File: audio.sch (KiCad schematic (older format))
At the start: 4 parts

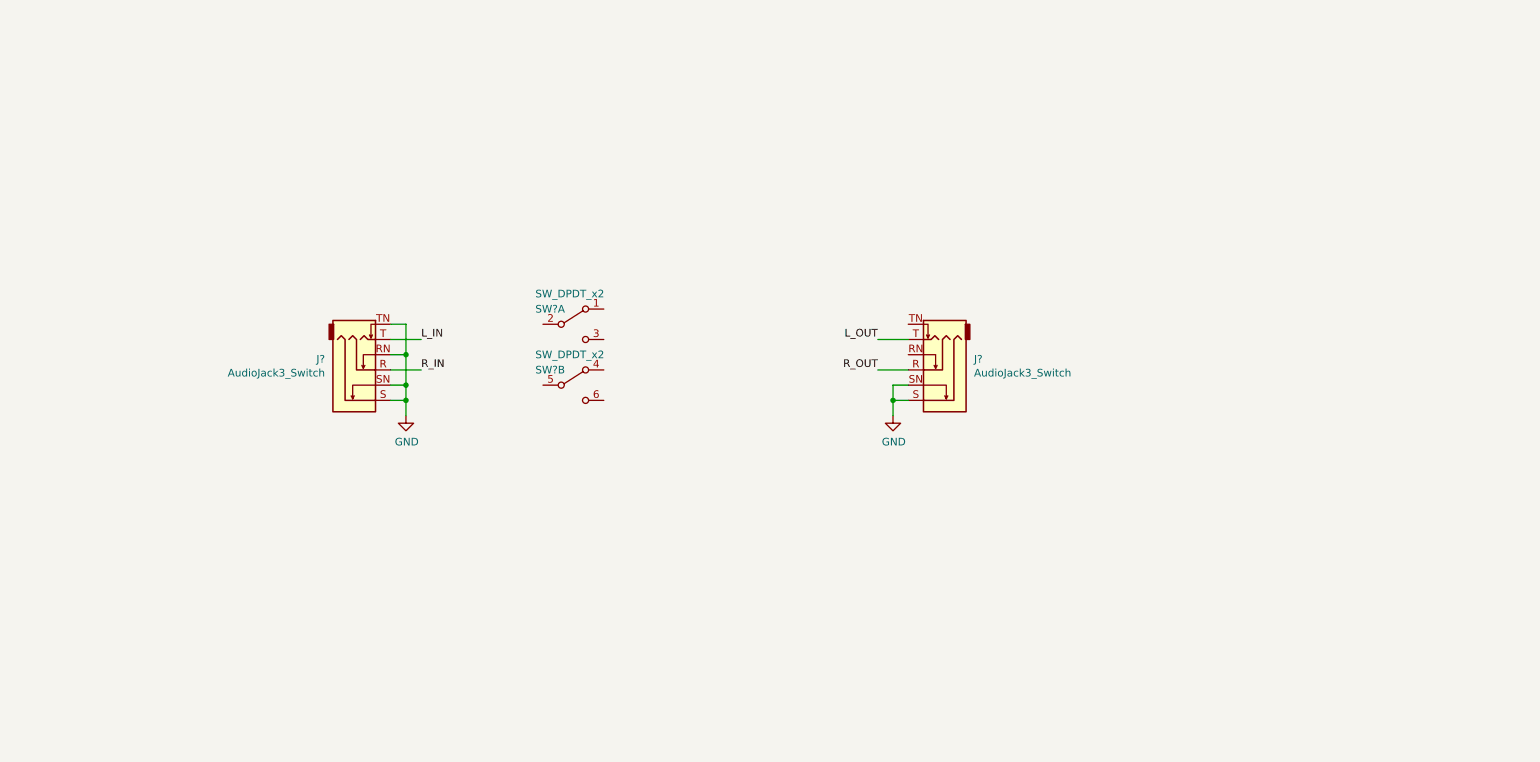
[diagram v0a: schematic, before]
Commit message: flesh out audio amp sheet, without R/C values
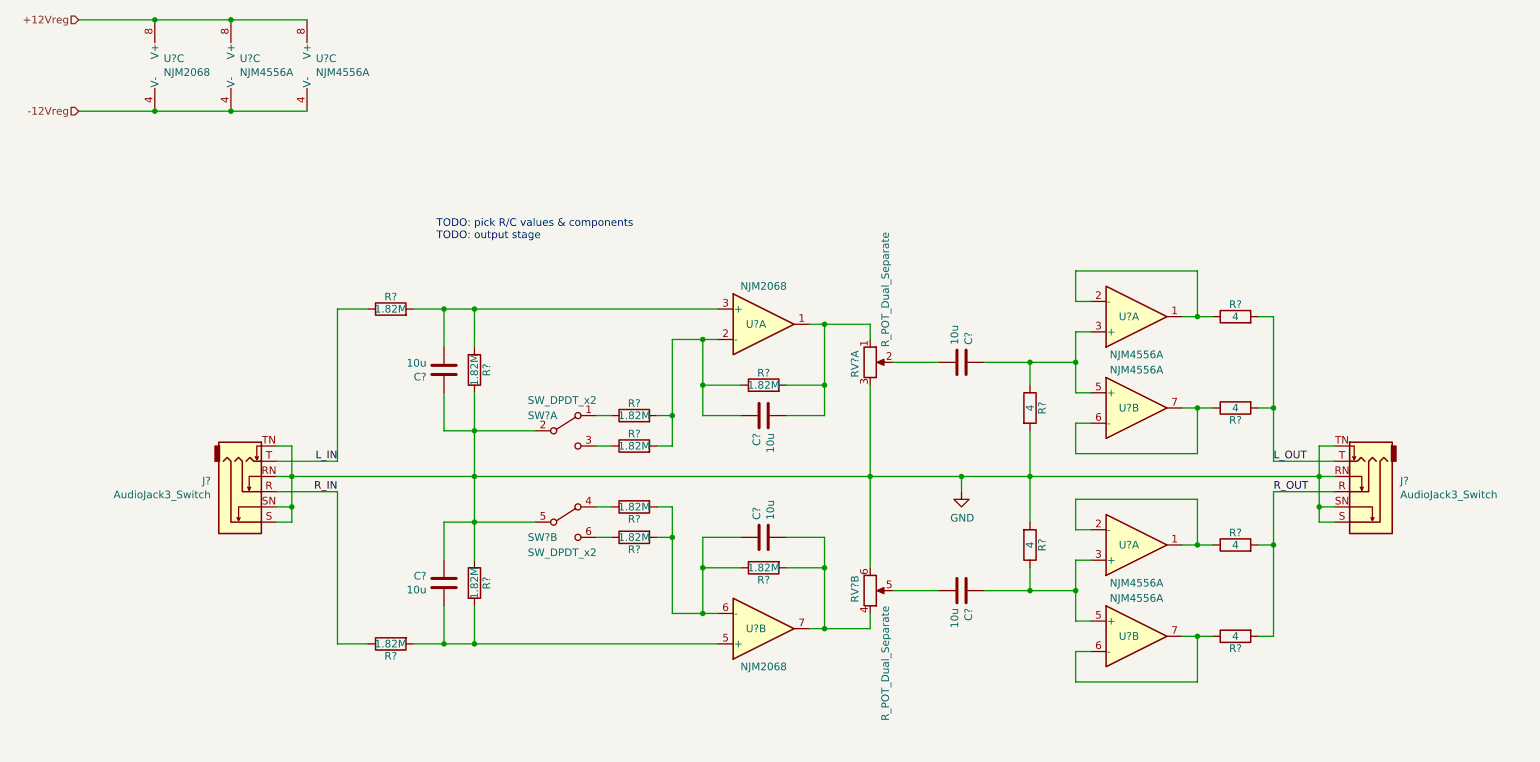
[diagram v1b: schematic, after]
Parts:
- added C? (x6): 10u, symbol Device:C
- added R? (x10): 1.82M, Resistor_SMD:R_0805_2012Metric_Pad1.15x1.40mm_HandSolder, symbol Device:R
- added R? (x6): 4, Resistor_SMD:R_0805_2012Metric_Pad1.15x1.40mm_HandSolder, symbol Device:R
- added RV? (x2): R_POT_Dual_Separate, symbol Device:R_POT_Dual_Separate
- added U? (x6): NJM4556A, symbol Amplifier_Operational:NJM4556A
- added U? (x3): NJM2068, symbol njr:NJM2068
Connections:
- net GND: now also J?.RN, J?.TN, SW?.2 (B), SW?.5 (B), C?.2, C?.2, R?.1, R?.1, R?.2, R?.2, RV?.3, RV?.6
- net L_IN: now also R?.1
- net L_OUT: now also R?.2, R?.2
- net R_IN: now also R?.1
- net R_OUT: now also R?.2, R?.2
- net at SW?.1 (A): now also R?.1
- net at SW?.3 (C): now also R?.1
- net at SW?.4 (A): now also R?.1
- net at SW?.6 (C): now also R?.1
- new net: R?.1, U?.1, U?.2 (-) (x2)
- new net: C?.2, R?.1, U?.3 (+), U?.5 (+) (x2)
- new net: R?.1, U?.6 (-), U?.7 (x2)
- new net: C?.1, R?.2, RV?.1, U?.1
- new net: C?.2, R?.1, R?.2, R?.2, U?.2 (-)
- new net: C?.1, R?.2, R?.2, U?.3 (+)
- new net: C?.1, R?.2, R?.2, U?.5 (+)
- new net: C?.2, R?.1, R?.2, R?.2, U?.6 (-)
- new net: C?.1, R?.2, RV?.4, U?.7
- new net: C?.1, RV?.2
- new net: C?.1, RV?.5
- new net +12Vreg: U?.8 (V+), U?.8 (V+), U?.8 (V+)
- new net -12Vreg: U?.4 (V-), U?.4 (V-), U?.4 (V-)
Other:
- note added: "TODO: pick R/C values & components\nTODO: output stage"
- moved on the sheet: J?, SW?A, SW?B

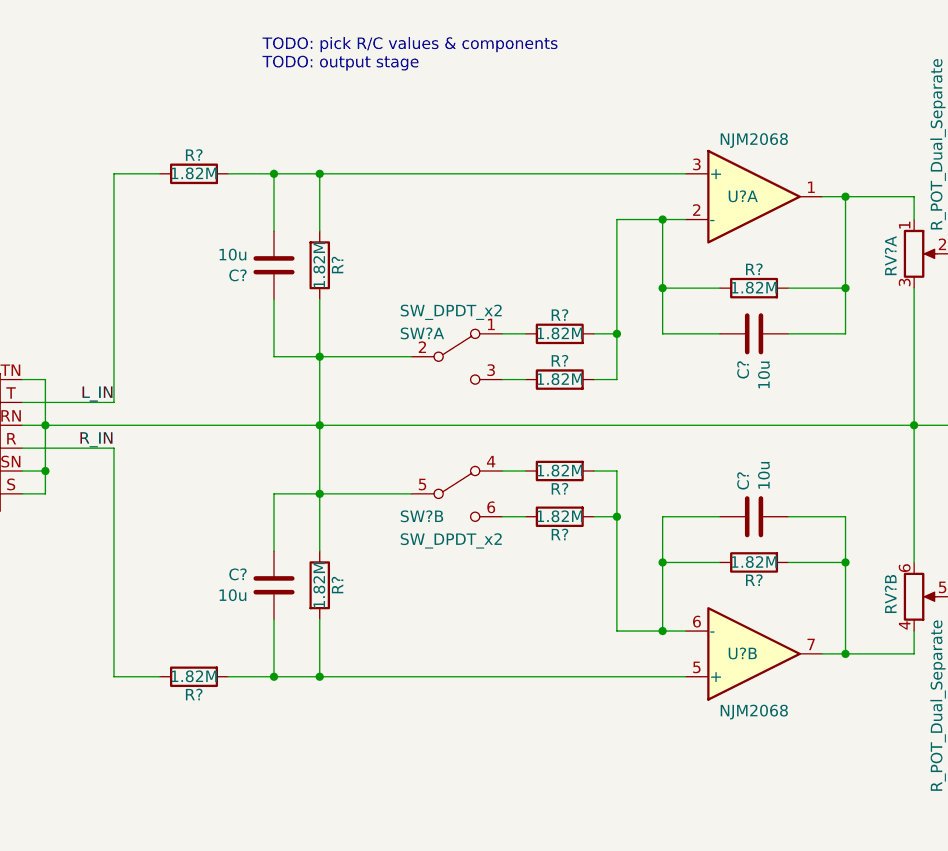
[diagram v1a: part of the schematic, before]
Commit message: add audio amp gain stage values
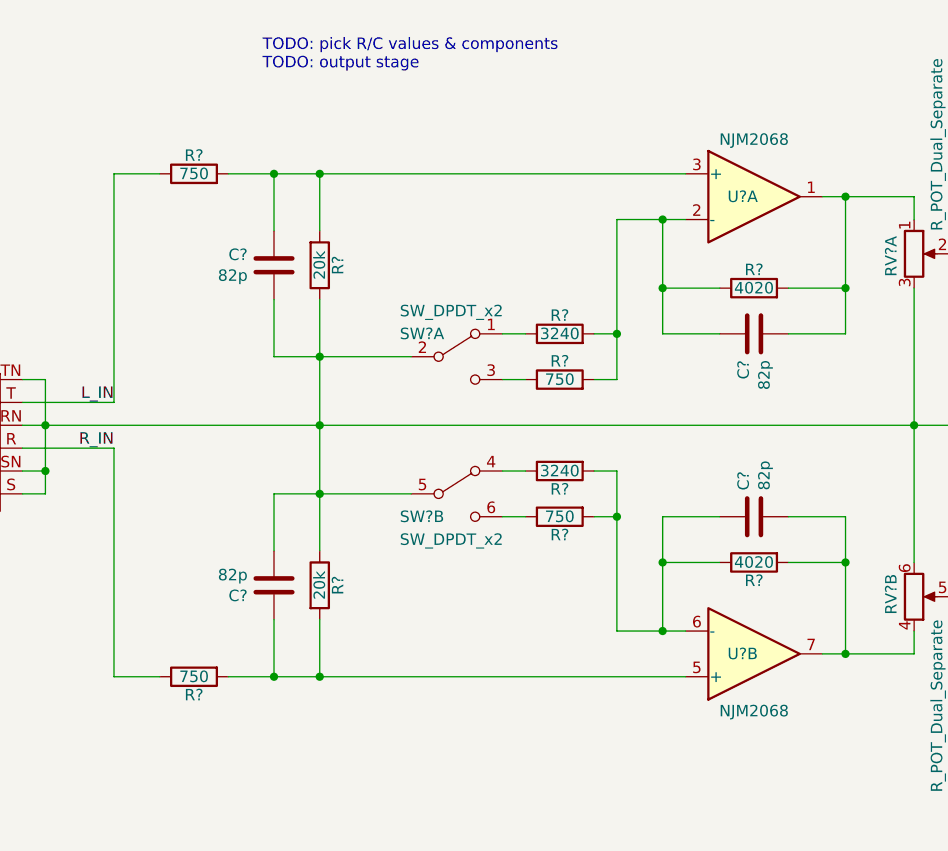
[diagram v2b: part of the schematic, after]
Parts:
- C? (x4): value 10u -> 82p
- R? (x2): value 1.82M -> 3240
- R? (x4): value 1.82M -> 750
- R? (x2): value 1.82M -> 4020
- R? (x2): value 1.82M -> 20k
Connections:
- net GND: now also C?.1, C?.1; no longer C?.2, C?.2
- net at R?.2, R?.2, U?.3 (+): now also C?.2; no longer C?.1
- net at R?.2, R?.2, U?.5 (+): now also C?.2; no longer C?.1
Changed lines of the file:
@@
 AR Path="/5CB56C16/5CE74784" Ref="R?"  Part="1"
 F 0 "R?" V 4830 3600 50  0000 C CNN
-F 1 "1.82M" V 4750 3600 50  0000 C CNN
+F 1 "3240" V 4750 3600 50  0000 C CNN
 F 2 "Resistor_SMD:R_0805_2012Metric_Pad1.15x1.40mm_HandSolder" V 4680 3600 50  0001 C CNN
 F 3 "https://industrial.panasonic.com/cdbs/www-data/pdf/RDA0000/AOA0000C304.pdf" H 4750 3600 50  0001 C CNN
@@
 AR Path="/5CB56C16/5CE74B22" Ref="R?"  Part="1"
 F 0 "R?" V 4830 3800 50  0000 C CNN
-F 1 "1.82M" V 4750 3800 50  0000 C CNN
+F 1 "750" V 4750 3800 50  0000 C CNN
 F 2 "Resistor_SMD:R_0805_2012Metric_Pad1.15x1.40mm_HandSolder" V 4680 3800 50  0001 C CNN
 F 3 "https://industrial.panasonic.com/cdbs/www-data/pdf/RDA0000/AOA0000C304.pdf" H 4750 3800 50  0001 C CNN
@@
 AR Path="/5CB56C16/5CE74BEC" Ref="R?"  Part="1"
 F 0 "R?" V 4830 4200 50  0000 C CNN
-F 1 "1.82M" V 4750 4200 50  0000 C CNN
+F 1 "3240" V 4750 4200 50  0000 C CNN
 F 2 "Resistor_SMD:R_0805_2012Metric_Pad1.15x1.40mm_HandSolder" V 4680 4200 50  0001 C CNN
 F 3 "https://industrial.panasonic.com/cdbs/www-data/pdf/RDA0000/AOA0000C304.pdf" H 4750 4200 50  0001 C CNN
@@
 AR Path="/5CB56C16/5CE74C54" Ref="R?"  Part="1"
 F 0 "R?" V 4830 4400 50  0000 C CNN
-F 1 "1.82M" V 4750 4400 50  0000 C CNN
+F 1 "750" V 4750 4400 50  0000 C CNN
 F 2 "Resistor_SMD:R_0805_2012Metric_Pad1.15x1.40mm_HandSolder" V 4680 4400 50  0001 C CNN
 F 3 "https://industrial.panasonic.com/cdbs/www-data/pdf/RDA0000/AOA0000C304.pdf" H 4750 4400 50  0001 C CNN
@@
 AR Path="/5CB56C16/5CE7733B" Ref="C?"  Part="1"
 F 0 "C?" H 5485 3554 50  0000 R CNN
-F 1 "10u" H 5485 3645 50  0000 R CNN
+F 1 "82p" H 5485 3645 50  0000 R CNN
 F 2 "" H 5638 3450 50  0001 C CNN
 F 3 "" H 5600 3600 50  0001 C CNN
@@
 AR Path="/5CB56C16/5CE77AE6" Ref="R?"  Part="1"
 F 0 "R?" V 5680 3400 50  0000 C CNN
-F 1 "1.82M" V 5600 3400 50  0000 C CNN
+F 1 "4020" V 5600 3400 50  0000 C CNN
 F 2 "Resistor_SMD:R_0805_2012Metric_Pad1.15x1.40mm_HandSolder" V 5530 3400 50  0001 C CNN
 F 3 "https://industrial.panasonic.com/cdbs/www-data/pdf/RDA0000/AOA0000C304.pdf" H 5600 3400 50  0001 C CNN
@@
 AR Path="/5CB56C16/5CE7D4D8" Ref="C?"  Part="1"
 F 0 "C?" H 5485 4354 50  0000 R CNN
-F 1 "10u" H 5485 4445 50  0000 R CNN
+F 1 "82p" H 5485 4445 50  0000 R CNN
 F 2 "" H 5638 4250 50  0001 C CNN
 F 3 "" H 5600 4400 50  0001 C CNN
@@
 AR Path="/5CB56C16/5CE7D4E4" Ref="R?"  Part="1"
 F 0 "R?" V 5680 4600 50  0000 C CNN
-F 1 "1.82M" V 5600 4600 50  0000 C CNN
+F 1 "4020" V 5600 4600 50  0000 C CNN
 F 2 "Resistor_SMD:R_0805_2012Metric_Pad1.15x1.40mm_HandSolder" V 5530 4600 50  0001 C CNN
 F 3 "https://industrial.panasonic.com/cdbs/www-data/pdf/RDA0000/AOA0000C304.pdf" H 5600 4600 50  0001 C CNN
@@
 AR Path="/5CB56C16/5CE8304A" Ref="C?"  Part="1"
 F 0 "C?" H 3385 3254 50  0000 R CNN
-F 1 "10u" H 3385 3345 50  0000 R CNN
+F 1 "82p" H 3385 3345 50  0000 R CNN
 F 2 "" H 3538 3150 50  0001 C CNN
 F 3 "" H 3500 3300 50  0001 C CNN
@@
 F 8 "" H 1050 -1850 50  0001 C CNN "Supplier Part Number"
 	1    3500 3300
-	1    0    0    -1
+	1    0    0    1
 $EndComp
 $Comp
@@
 AR Path="/5CB56C16/5CE83056" Ref="R?"  Part="1"
 F 0 "R?" V 3780 3300 50  0000 C CNN
-F 1 "1.82M" V 3700 3300 50  0000 C CNN
+F 1 "20k" V 3700 3300 50  0000 C CNN
 F 2 "Resistor_SMD:R_0805_2012Metric_Pad1.15x1.40mm_HandSolder" V 3630 3300 50  0001 C CNN
 F 3 "https://industrial.panasonic.com/cdbs/www-data/pdf/RDA0000/AOA0000C304.pdf" H 3700 3300 50  0001 C CNN
@@
 AR Path="/5CB56C16/5CE86205" Ref="R?"  Part="1"
 F 0 "R?" V 3230 2900 50  0000 C CNN
-F 1 "1.82M" V 3150 2900 50  0000 C CNN
+F 1 "750" V 3150 2900 50  0000 C CNN
 F 2 "Resistor_SMD:R_0805_2012Metric_Pad1.15x1.40mm_HandSolder" V 3080 2900 50  0001 C CNN
 F 3 "https://industrial.panasonic.com/cdbs/www-data/pdf/RDA0000/AOA0000C304.pdf" H 3150 2900 50  0001 C CNN
@@
 AR Path="/5CB56C16/5CE8BC3D" Ref="C?"  Part="1"
 F 0 "C?" H 3385 4654 50  0000 R CNN
-F 1 "10u" H 3385 4745 50  0000 R CNN
+F 1 "82p" H 3385 4745 50  0000 R CNN
 F 2 "" H 3538 4550 50  0001 C CNN
 F 3 "" H 3500 4700 50  0001 C CNN
@@
 F 8 "" H 1050 -450 50  0001 C CNN "Supplier Part Number"
 	1    3500 4700
-	1    0    0    1
+	1    0    0    -1
 $EndComp
 $Comp
@@
 AR Path="/5CB56C16/5CE8BC49" Ref="R?"  Part="1"
 F 0 "R?" V 3780 4700 50  0000 C CNN
-F 1 "1.82M" V 3700 4700 50  0000 C CNN
+F 1 "20k" V 3700 4700 50  0000 C CNN
 F 2 "Resistor_SMD:R_0805_2012Metric_Pad1.15x1.40mm_HandSolder" V 3630 4700 50  0001 C CNN
 F 3 "https://industrial.panasonic.com/cdbs/www-data/pdf/RDA0000/AOA0000C304.pdf" H 3700 4700 50  0001 C CNN
@@
 AR Path="/5CB56C16/5CE8BC59" Ref="R?"  Part="1"
 F 0 "R?" V 3230 5100 50  0000 C CNN
-F 1 "1.82M" V 3150 5100 50  0000 C CNN
+F 1 "750" V 3150 5100 50  0000 C CNN
 F 2 "Resistor_SMD:R_0805_2012Metric_Pad1.15x1.40mm_HandSolder" V 3080 5100 50  0001 C CNN
 F 3 "https://industrial.panasonic.com/cdbs/www-data/pdf/RDA0000/AOA0000C304.pdf" H 3150 5100 50  0001 C CNN

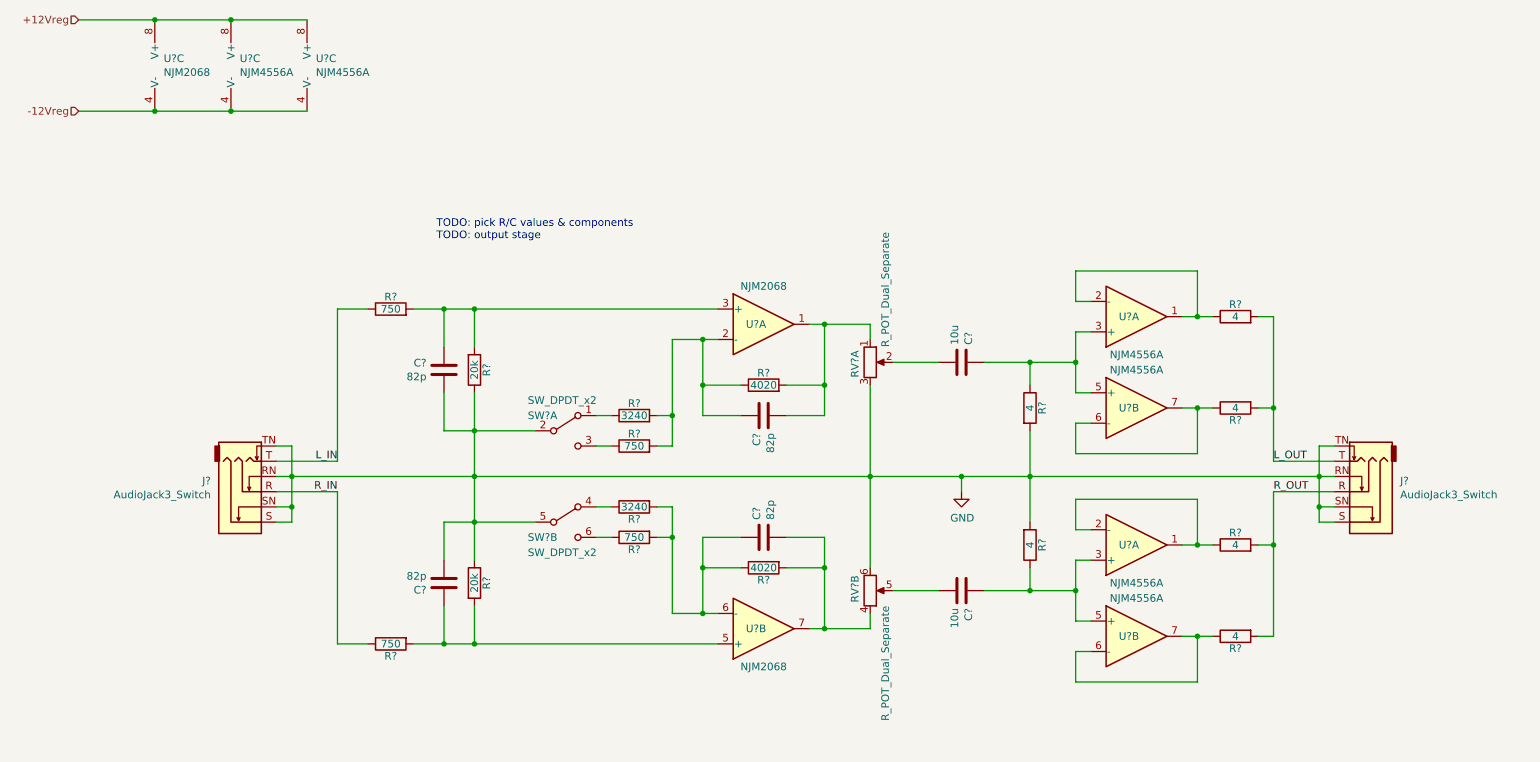
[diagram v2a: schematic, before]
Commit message: add audio amp output stage values
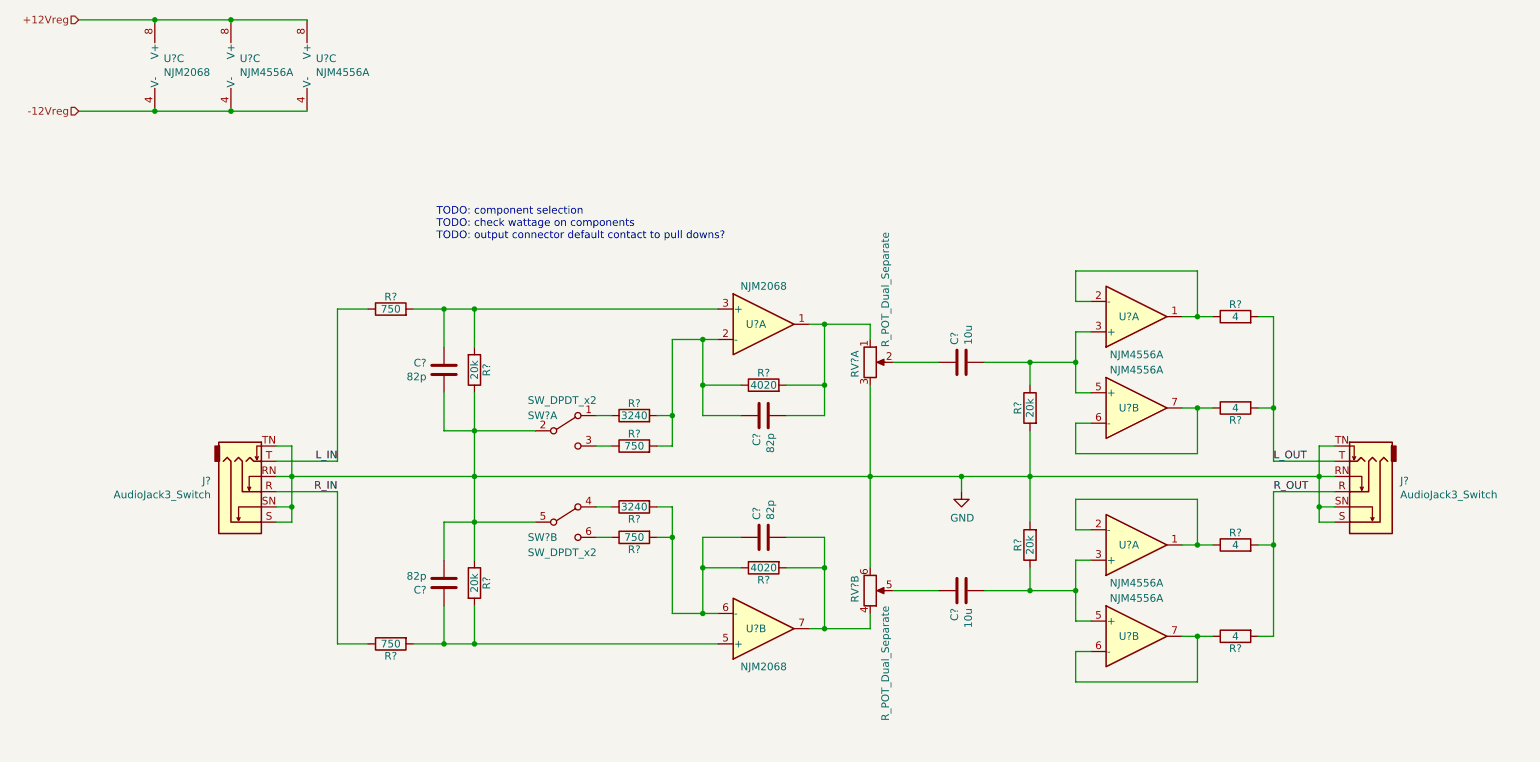
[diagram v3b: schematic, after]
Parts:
- R? (x2): value 4 -> 20k
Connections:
- net at R?.1, U?.3 (+), U?.5 (+): now also C?.1; no longer C?.2 (x2)
- net at RV?.2: now also C?.2; no longer C?.1
- net at RV?.5: now also C?.2; no longer C?.1
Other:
- note added: "TODO: component selection\nTODO: check wattage on components\nTODO: output connector default contact to pull downs?"
- note removed: "TODO: pick R/C values & components\nTODO: output stage"
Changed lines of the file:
@@
 	3700 4000 3700 4300
 Text Notes 3450 2450 0    50   ~ 0
-TODO: pick R/C values & components\nTODO: output stage
+TODO: component selection\nTODO: check wattage on components\nTODO: output connector default contact to pull downs?
 $Comp
 L Amplifier_Operational:NJM4556A U?
@@
 F 8 "" H 4450 -1900 50  0001 C CNN "Supplier Part Number"
 	1    6900 3250
-	0    -1   1    0
+	0    1    1    0
 $EndComp
 $Comp
@@
 AR Path="/5CB56C16/5CEDAB07" Ref="R?"  Part="1"
 F 0 "R?" V 7430 3550 50  0000 C CNN
-F 1 "4" V 7350 3550 50  0000 C CNN
+F 1 "20k" V 7350 3550 50  0000 C CNN
 F 2 "Resistor_SMD:R_0805_2012Metric_Pad1.15x1.40mm_HandSolder" V 7280 3550 50  0001 C CNN
 F 3 "https://industrial.panasonic.com/cdbs/www-data/pdf/RDA0000/AOA0000C304.pdf" H 7350 3550 50  0001 C CNN
@@
 F 8 "P1.82BTCT-ND" H 7350 3550 50  0001 C CNN "Supplier Part Number"
 	1    7350 3550
-	1    0    0    -1
+	-1   0    0    -1
 $EndComp
 Wire Wire Line
@@
 F 8 "" H 4450 -400 50  0001 C CNN "Supplier Part Number"
 	1    6900 4750
-	0    -1   -1   0
+	0    1    -1   0
 $EndComp
 $Comp
@@
 AR Path="/5CB56C16/5CEE5E17" Ref="R?"  Part="1"
 F 0 "R?" V 7430 4450 50  0000 C CNN
-F 1 "4" V 7350 4450 50  0000 C CNN
+F 1 "20k" V 7350 4450 50  0000 C CNN
 F 2 "Resistor_SMD:R_0805_2012Metric_Pad1.15x1.40mm_HandSolder" V 7280 4450 50  0001 C CNN
 F 3 "https://industrial.panasonic.com/cdbs/www-data/pdf/RDA0000/AOA0000C304.pdf" H 7350 4450 50  0001 C CNN
@@
 F 8 "P1.82BTCT-ND" H 7350 4450 50  0001 C CNN "Supplier Part Number"
 	1    7350 4450
-	1    0    0    1
-$EndComp
-Wire Wire Line
+	-1   0    0    1
+$EndComp
+Wire Wire Line
